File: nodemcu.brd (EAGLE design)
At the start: 50.5 x 49.5 mm, 6 parts

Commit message: uprava desky
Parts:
- moved SL1 29.0 mm to (29.2, 43.2), turned to 270 degrees
- moved D1 7.62 mm to (35.6, 12.7)
- moved SL2 6.35 mm to (40.6, 12.7)
- moved X1 4.02 mm to (38.1, 41.9)
- moved SENSOR 3.81 mm to (34.3, 30.5)
- moved U$1 2.54 mm to (14.0, 24.1)
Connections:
- new net N$6: U$1.VIN
- net +3V3: now also U$1.3V3@2; no longer U$1.VIN
- net GND: now also U$1.GND@3; no longer U$1.GND@1
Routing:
- net N$4: track 15.2 -> 59.7 mm
- net +3V3: track 83.8 -> 48.3 mm
- net GND: track 75.6 -> 42.5 mm
- net N$1: track 35.6 -> 3.81 mm
- net N$2: track 15.2 -> 14.0 mm
- net N$3: track 22.9 -> 21.6 mm
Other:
- board size 50.5 x 49.5 mm -> 44.1 x 48.2 mm

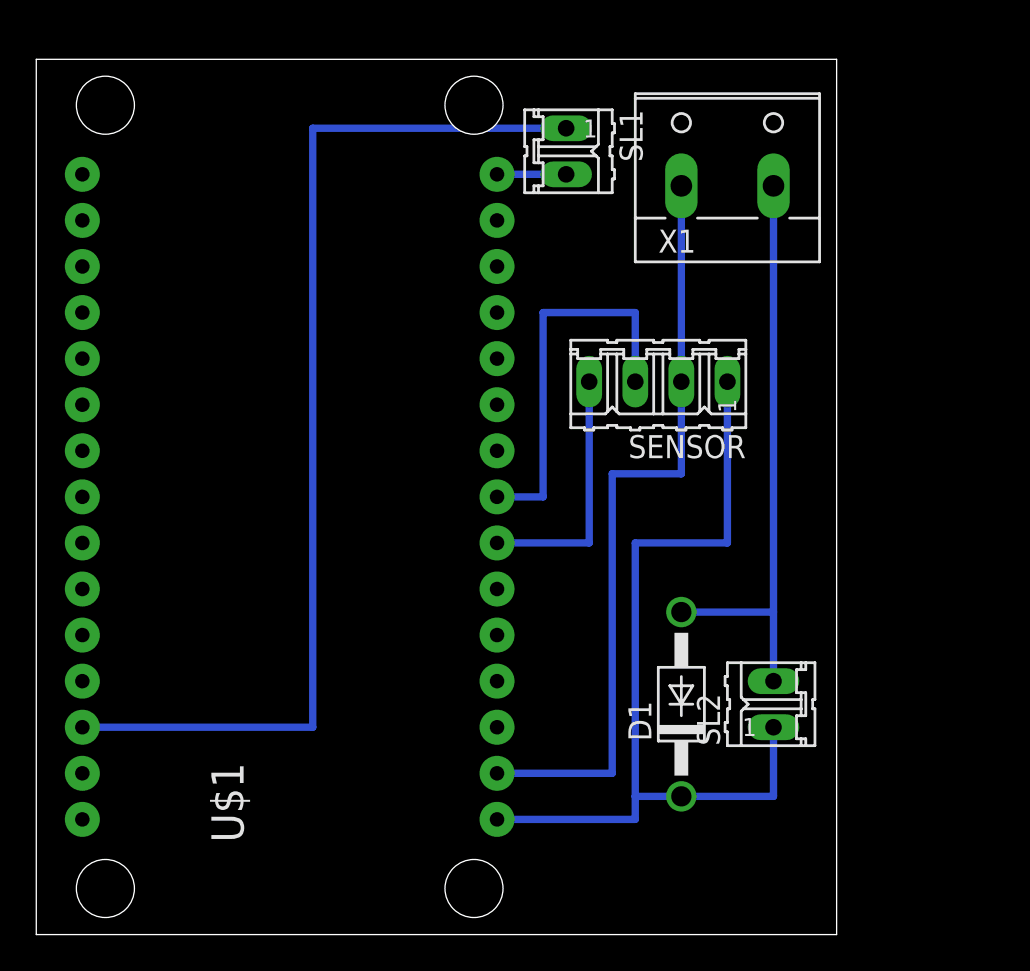
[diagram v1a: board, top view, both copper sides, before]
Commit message: upraveno schema pro dip switch
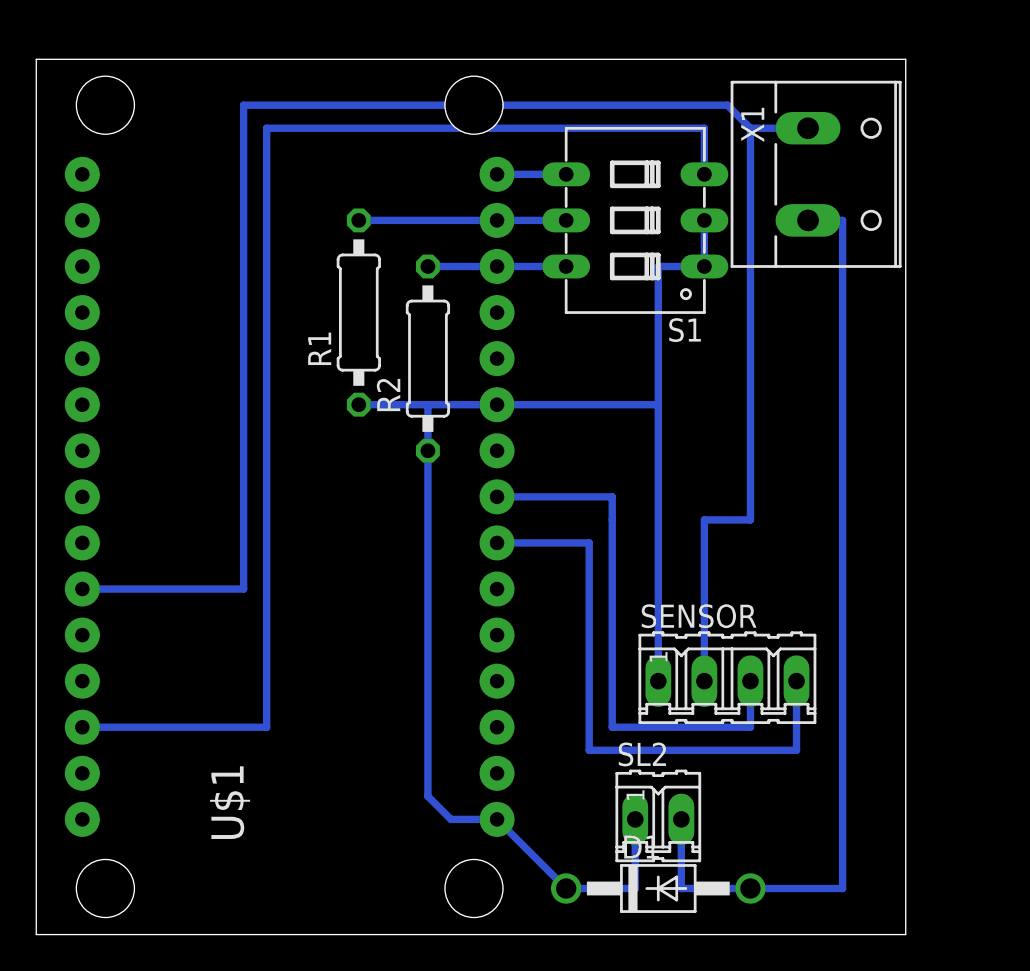
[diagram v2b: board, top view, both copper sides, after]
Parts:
- removed SL1: (no value), con-amp-quick:02P
- added R1, R2: 10k, rcl:0207/10
- added S1: (no value), switch-dil:DIP03YL
- moved SENSOR 16.9 mm to (38.1, 14.0), turned to 0 degrees
- moved D1 10.2 mm to (34.3, 2.54), turned to 0 degrees
- moved SL2 8.98 mm to (34.3, 6.35), turned to 0 degrees
- moved X1 5.08 mm to (43.2, 41.9), turned to 270 degrees
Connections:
- removed net N$6: U$1.VIN
- new net N$8: R1.2, S1.5, U$1.D1
- new net N$9: R2.2, S1.6, U$1.D2
- net +3V3: now also R1.1, R2.1, S1.1, S1.2, U$1.3V3@1
- net GND: now also U$1.GND@0; no longer U$1.GND@3
- net N$1: now also S1.4; no longer SL1.2
- net N$4: now also S1.3; no longer SL1.1
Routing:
- net GND: track 42.5 -> 100.2 mm
- net +3V3: track 48.3 -> 83.4 mm
- net N$5: track 32.4 -> 51.4 mm
- net N$2: track 14.0 -> 31.7 mm
- net N$8: track 0.00 -> 11.4 mm
- net N$4: track 59.7 -> 69.9 mm
- net N$9: track 0.00 -> 7.62 mm
- net N$3: track 21.6 -> 29.2 mm
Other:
- board size 44.1 x 48.2 mm -> 47.9 x 48.2 mm

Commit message: upravy spoje
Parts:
- moved R1 2.54 mm to (15.2, 34.3)
- moved R2 2.54 mm to (19.1, 31.8)
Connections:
- net +3V3: no longer S1.1, S1.2
- net GND: now also S1.1, S1.2
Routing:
- net +3V3: track 83.4 -> 76.5 mm
- net GND: track 100.2 -> 105.3 mm
- net N$8: track 11.4 -> 14.0 mm
- net N$9: track 7.62 -> 10.2 mm
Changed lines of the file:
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@@
 <?xml version="1.0" encoding="utf-8"?>
 <!DOCTYPE eagle SYSTEM "eagle.dtd">
-<eagle version="7.3.0">
+<eagle version="7.7.0">
 <drawing>
 <settings>
@@
 <attribute name="MPN" value="" x="33.02" y="39.37" size="1.778" layer="27" rot="R90" display="off"/>
 </element>
-<element name="R1" library="rcl" package="0207/10" value="10k" x="17.78" y="34.29" rot="R90"/>
-<element name="R2" library="rcl" package="0207/10" value="10k" x="21.59" y="31.75" rot="R90"/>
+<element name="R1" library="rcl" package="0207/10" value="10k" x="15.24" y="34.29" rot="R90"/>
+<element name="R2" library="rcl" package="0207/10" value="10k" x="19.05" y="31.75" rot="R90"/>
 </elements>
 <signals>
@@
 <contactref element="U$1" pad="3V3@2"/>
 <wire x1="29.21" y1="2.54" x2="25.4" y2="6.35" width="0.4064" layer="16"/>
-<contactref element="S1" pad="1"/>
-<contactref element="R1" pad="1"/>
-<contactref element="S1" pad="2"/>
-<contactref element="R2" pad="1"/>
-<contactref element="U$1" pad="3V3@1"/>
-<wire x1="25.4" y1="6.35" x2="22.86" y2="6.35" width="0.4064" layer="16"/>
-<wire x1="22.86" y1="6.35" x2="21.59" y2="7.62" width="0.4064" layer="16"/>
-<wire x1="21.59" y1="7.62" x2="21.59" y2="26.67" width="0.4064" layer="16"/>
-<wire x1="34.29" y1="13.97" x2="34.29" y2="29.21" width="0.4064" layer="16"/>
-<wire x1="34.29" y1="29.21" x2="34.29" y2="36.83" width="0.4064" layer="16"/>
-<wire x1="34.29" y1="36.83" x2="36.83" y2="36.83" width="0.4064" layer="16"/>
-<wire x1="25.4" y1="29.21" x2="34.29" y2="29.21" width="0.4064" layer="16"/>
 <wire x1="29.21" y1="2.54" x2="33.02" y2="2.54" width="0.4064" layer="16"/>
 <wire x1="33.02" y1="2.54" x2="33.02" y2="6.35" width="0.4064" layer="16"/>
-<wire x1="25.4" y1="29.21" x2="21.59" y2="29.21" width="0.4064" layer="16"/>
-<wire x1="21.59" y1="29.21" x2="17.78" y2="29.21" width="0.4064" layer="16"/>
-<wire x1="21.59" y1="26.67" x2="21.59" y2="29.21" width="0.4064" layer="16"/>
-<wire x1="36.83" y1="36.83" x2="36.83" y2="39.37" width="0.4064" layer="16"/>
+<contactref element="R1" pad="1"/>
+<contactref element="R2" pad="1"/>
+<wire x1="19.05" y1="29.21" x2="15.24" y2="29.21" width="0.4064" layer="16"/>
+<wire x1="19.05" y1="26.67" x2="19.05" y2="29.21" width="0.4064" layer="16"/>
+<wire x1="34.29" y1="29.21" x2="34.29" y2="13.97" width="0.4064" layer="16"/>
+<contactref element="U$1" pad="3V3@1"/>
+<wire x1="19.05" y1="29.21" x2="25.4" y2="29.21" width="0.4064" layer="16"/>
+<wire x1="25.4" y1="29.21" x2="34.29" y2="29.21" width="0.4064" layer="16"/>
+<wire x1="25.4" y1="6.35" x2="19.05" y2="6.35" width="0.4064" layer="16"/>
+<wire x1="19.05" y1="6.35" x2="19.05" y2="26.67" width="0.4064" layer="16"/>
 </signal>
 <signal name="GND">
@@
 <contactref element="X1" pad="1"/>
 <wire x1="42.545" y1="44.45" x2="39.37" y2="44.45" width="0.4064" layer="16"/>
-<wire x1="39.37" y1="44.45" x2="39.37" y2="22.86" width="0.4064" layer="16"/>
+<wire x1="39.37" y1="44.45" x2="39.37" y2="39.37" width="0.4064" layer="16"/>
+<wire x1="39.37" y1="39.37" x2="39.37" y2="22.86" width="0.4064" layer="16"/>
 <wire x1="39.37" y1="22.86" x2="36.83" y2="22.86" width="0.4064" layer="16"/>
 <wire x1="36.83" y1="22.86" x2="36.83" y2="13.97" width="0.4064" layer="16"/>
@@
 <wire x1="11.43" y1="45.72" x2="38.1" y2="45.72" width="0.4064" layer="16"/>
 <wire x1="38.1" y1="45.72" x2="39.37" y2="44.45" width="0.4064" layer="16"/>
+<contactref element="S1" pad="1"/>
+<contactref element="S1" pad="2"/>
+<wire x1="36.83" y1="36.83" x2="36.83" y2="39.37" width="0.4064" layer="16"/>
+<wire x1="36.83" y1="39.37" x2="39.37" y2="39.37" width="0.4064" layer="16"/>
 </signal>
 <signal name="N$1">
@@
 <contactref element="S1" pad="5"/>
 <contactref element="R1" pad="2"/>
-<wire x1="25.4" y1="39.37" x2="17.78" y2="39.37" width="0.4064" layer="16"/>
+<wire x1="25.4" y1="39.37" x2="15.24" y2="39.37" width="0.4064" layer="16"/>
 <wire x1="25.4" y1="39.37" x2="29.21" y2="39.37" width="0.4064" layer="16"/>
 </signal>
@@
 <contactref element="S1" pad="6"/>
 <contactref element="R2" pad="2"/>
-<wire x1="25.4" y1="36.83" x2="21.59" y2="36.83" width="0.4064" layer="16"/>
+<wire x1="25.4" y1="36.83" x2="19.05" y2="36.83" width="0.4064" layer="16"/>
 <wire x1="25.4" y1="36.83" x2="29.21" y2="36.83" width="0.4064" layer="16"/>
 </signal>
